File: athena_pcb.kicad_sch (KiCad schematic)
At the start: 29 parts, among them J1 Conn_02x03_Odd_Even, SW1 SW_Push, U1 NRF5340-QKAA-R7, U2 BME280, Y1 32MHz, Y2 32.768kHz

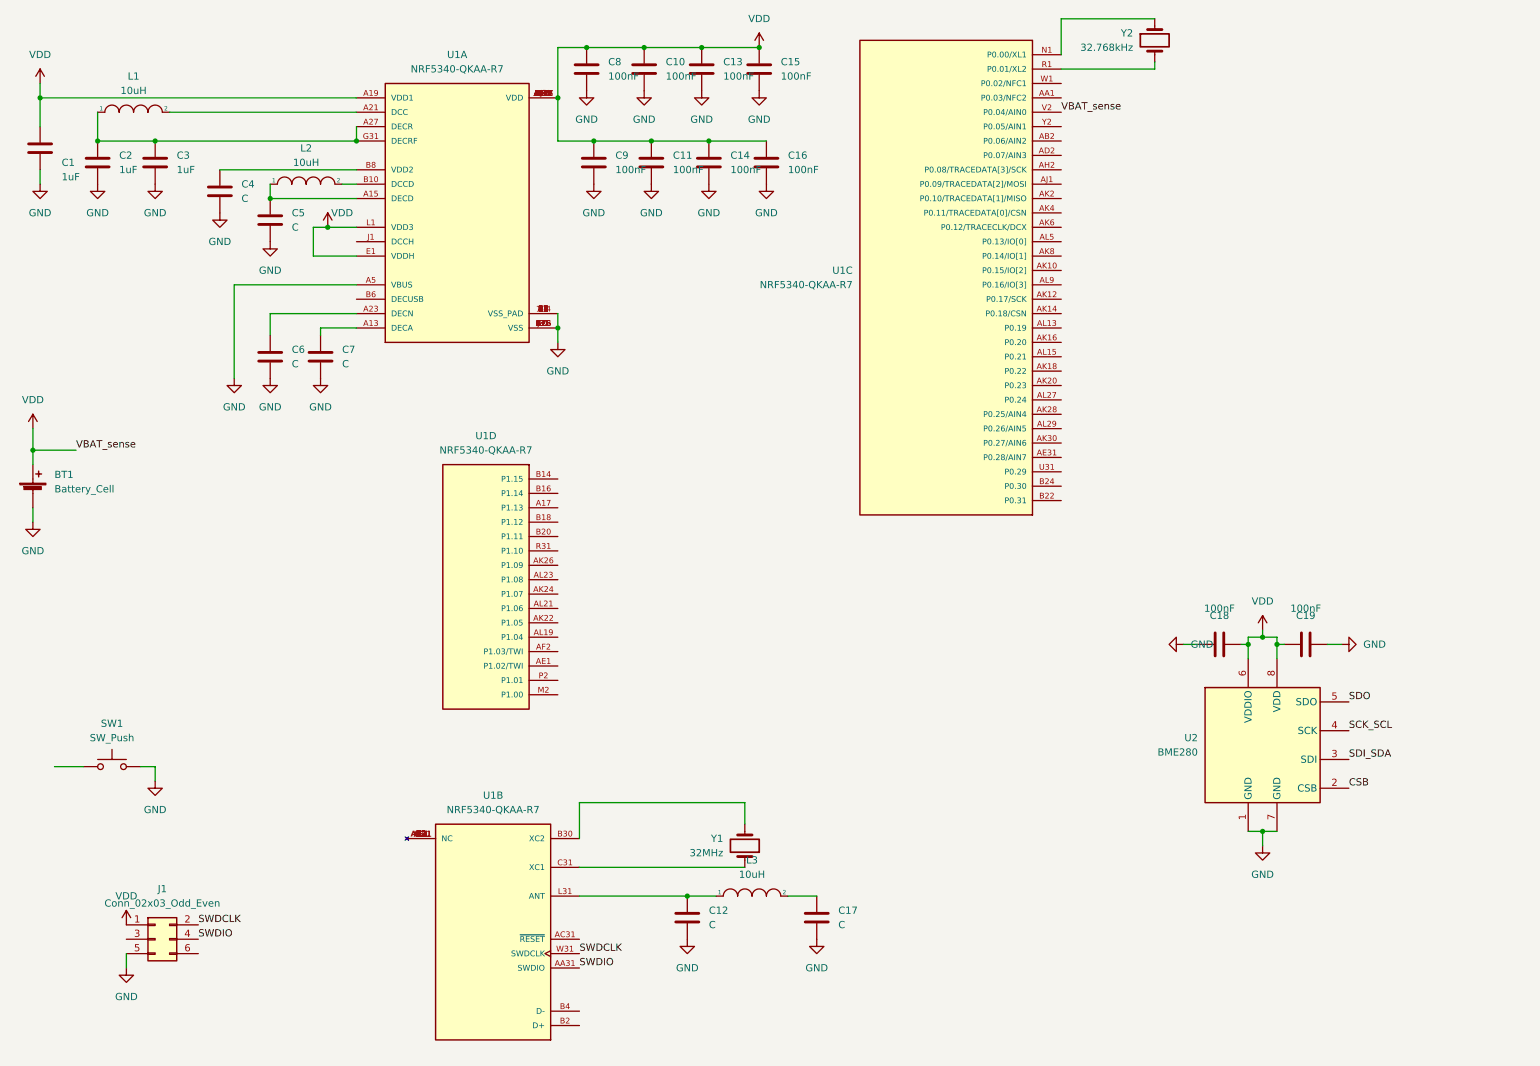
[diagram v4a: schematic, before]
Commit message: Added user button and indicator LED
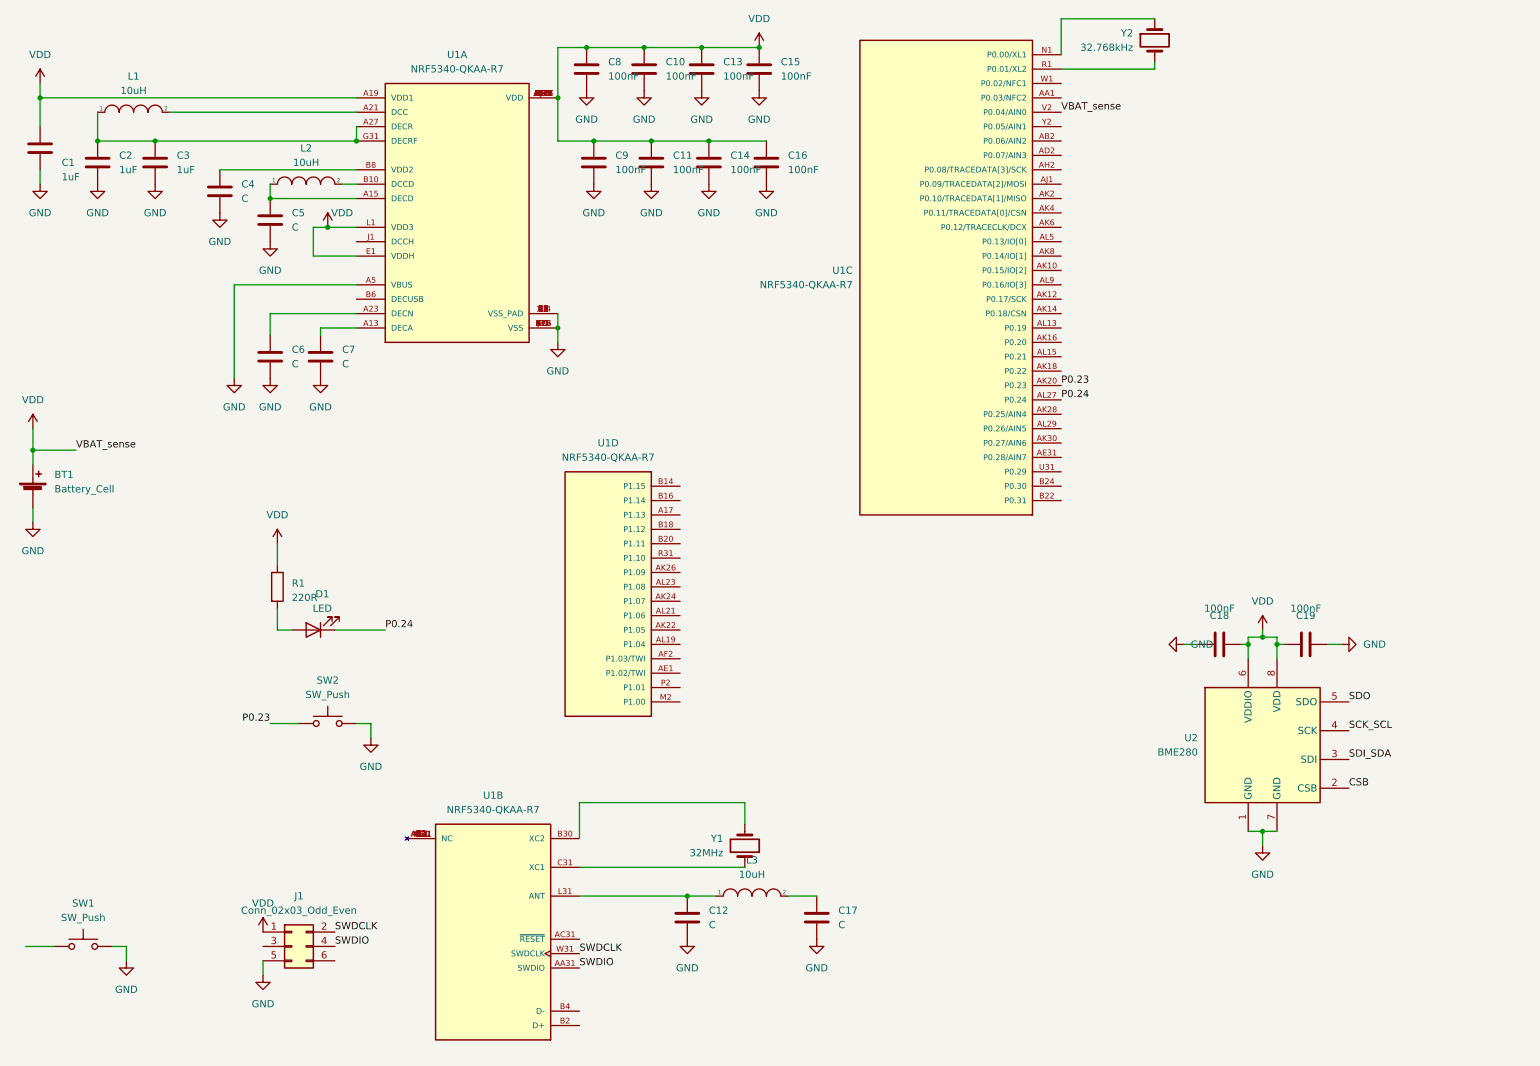
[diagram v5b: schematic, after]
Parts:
- added D1: LED, symbol Device:LED
- added R1: 220R, symbol Device:R
- added SW2: SW_Push, symbol Switch:SW_Push
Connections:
- net GND: now also SW2.2
- net VDD: now also R1.1
- net P0.23: now reaches U1.AK20 (P0.23)
- net P0.23: now also SW2.1
- net P0.24: now reaches U1.AL27 (P0.24)
- net P0.24: now also D1.1 (K)
- new net: D1.2 (A), R1.2
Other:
- moved on the sheet: J1, SW1, U1D

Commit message: Added footprint to capacitors
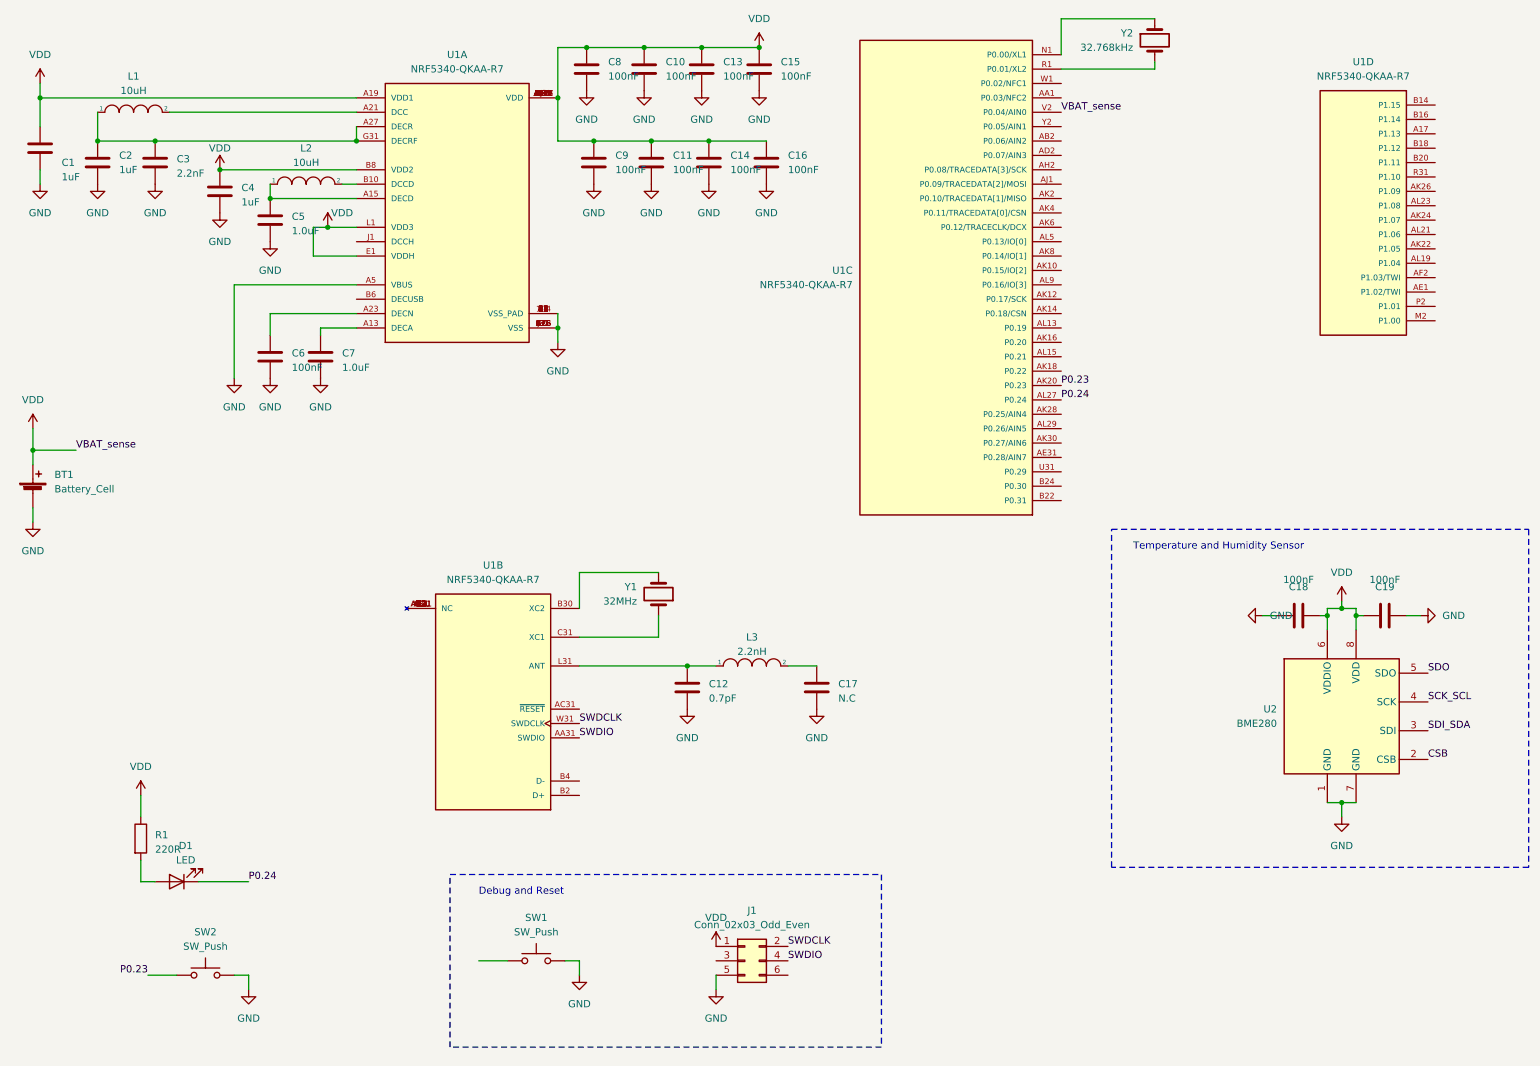
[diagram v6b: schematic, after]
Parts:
- C1, C2, C9: footprint (none) -> Capacitor_SMD:C_0402_1005Metric
- C10, C11, C13, C14, C15, C16, C18, C19, C8: footprint (none) -> Capacitor_SMD:C_0201_0603Metric
- C12: value C -> 0.7pF; footprint (none) -> Capacitor_SMD:C_0201_0603Metric
- C17: value C -> N.C; footprint (none) -> Capacitor_SMD:C_0201_0603Metric
- C3: value 1uF -> 2.2nF; footprint (none) -> Capacitor_SMD:C_0201_0603Metric
- C4: value C -> 1uF; footprint (none) -> Capacitor_SMD:C_0402_1005Metric
- C5, C7: value C -> 1.0uF; footprint (none) -> Capacitor_SMD:C_0402_1005Metric
- C6: value C -> 100nF; footprint (none) -> Capacitor_SMD:C_0201_0603Metric
- L3: value 10uH -> 2.2nH; footprint (none) -> Inductor_SMD:L_0201_0603Metric
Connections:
- net VDD: now also C4.1, U1.B8 (VDD2)
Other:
- note added: "Debug and Reset"
- note added: "Temperature and Humidity Sensor"
- moved on the sheet: C12, C17, C18, C19, D1, J1, L3, R1, SW1, SW2, U1B, U1D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

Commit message: Added footprint and symbol for the NRF53
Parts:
- BT1: footprint (none) -> Battery:BatteryHolder_Keystone_1060_1x2032
- D1: footprint (none) -> LED_SMD:LED_0402_1005Metric
- J1: footprint (none) -> Connector_PinHeader_1.27mm:PinHeader_2x03_P1.27mm_Vertical
- L1, L2: footprint (none) -> Inductor_SMD:L_0201_0603Metric
- R1: footprint (none) -> Resistor_SMD:R_0201_0603Metric
- SW1: footprint (none) -> Button_Switch_SMD:SW_Push_SPST_NO_Alps_SKRK
- SW2: footprint (none) -> Button_Switch_SMD:SW_Push_1P1T_NO_CK_KMR2
- Y1: footprint (none) -> Crystal:Crystal_SMD_2016-4Pin_2.0x1.6mm
- Y2: footprint (none) -> Crystal:Crystal_SMD_2012-2Pin_2.0x1.2mm
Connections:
- no-connect marks 0 -> 5
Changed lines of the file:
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@@
   (junction (at 116.84 19.05) (diameter 0) (color 0 0 0 0)
   )
+  (junction (at 111.76 71.12) (diameter 0) (color 0 0 0 0)
+  )
   (junction (at 52.07 40.64) (diameter 0) (color 0 0 0 0)
   )
@@
   (junction (at 19.05 90.17) (diameter 0) (color 0 0 0 0)
   )
+  (no_connect (at 76.2 63.5))
+  (no_connect (at 139.7 180.34))
+  (no_connect (at 76.2 53.34))
+  (no_connect (at 115.57 148.59))
+  (no_connect (at 115.57 151.13))
   (wire (pts (xy 200.66 22.86) (xy 217.17 22.86))
     (stroke (width 0) (type default))
@@
     (stroke (width 0) (type default))
   )
+  (wire (pts (xy 111.76 71.12) (xy 119.38 71.12))
+    (stroke (width 0) (type default))
+  )
   (wire (pts (xy 115.57 111.76) (xy 129.54 111.76))
     (stroke (width 0) (type default))
@@
     (stroke (width 0) (type default))
   )
+  (wire (pts (xy 57.15 110.49) (xy 57.15 114.3))
+    (stroke (width 0) (type default))
+  )
   (wire (pts (xy 128.27 35.56) (xy 138.43 35.56))
     (stroke (width 0) (type default))
@@
   )
   (wire (pts (xy 247.65 118.11) (xy 250.19 118.11))
+    (stroke (width 0) (type default))
+  )
+  (wire (pts (xy 48.26 105.41) (xy 48.26 109.22))
     (stroke (width 0) (type default))
   )
@@
     )
   )
+  (symbol (lib_id "power:PWR_FLAG") (at 119.38 71.12 270) (unit 1)
+    (in_bom yes) (on_board yes) (dnp no) (fields_autoplaced)
+    (property "Reference" "#FLG02" (at 121.285 71.12 0)
+      (effects (font (size 1.27 1.27)) hide)
+    )
+    (property "Value" "PWR_FLAG" (at 123.19 71.755 90)
+      (effects (font (size 1.27 1.27)) (justify left))
+    )
+    (property "Footprint" "" (at 119.38 71.12 0)
+      (effects (font (size 1.27 1.27)) hide)
+    )
+    (property "Datasheet" "~" (at 119.38 71.12 0)
+      (effects (font (size 1.27 1.27)) hide)
+    )
+    (pin "1")
+    (instances
+      (project "athena_pcb"
+        (path "/fadb6411-1081-41a3-ba72-837bcce93ee0"
+          (reference "#FLG02") (unit 1)
+        )
+      )
+    )
+  )
   (symbol (lib_id "power:GND") (at 148.59 43.18 0) (unit 1)
     (in_bom yes) (on_board yes) (dnp no) (fields_autoplaced)
@@
       (effects (font (size 1.27 1.27)))
     )
-    (property "Footprint" "" (at 67.31 43.18 0)
+    (property "Footprint" "Inductor_SMD:L_0201_0603Metric" (at 67.31 43.18 0)
       (effects (font (size 1.27 1.27)) hide)
     )
@@
       (effects (font (size 1.27 1.27)) (justify left))
     )
-    (property "Footprint" "" (at 19.05 96.266 90)
+    (property "Footprint" "Battery:BatteryHolder_Keystone_1060_1x2032" (at 19.05 96.266 90)
       (effects (font (size 1.27 1.27)) hide)
     )
@@
         (path "/fadb6411-1081-41a3-ba72-837bcce93ee0"
           (reference "BT1") (unit 1)
+        )
+      )
+    )
+  )
+  (symbol (lib_id "power:PWR_FLAG") (at 48.26 105.41 0) (unit 1)
+    (in_bom yes) (on_board yes) (dnp no) (fields_autoplaced)
+    (property "Reference" "#FLG03" (at 48.26 103.505 0)
+      (effects (font (size 1.27 1.27)) hide)
+    )
+    (property "Value" "PWR_FLAG" (at 48.26 101.6 0)
+      (effects (font (size 1.27 1.27)))
+    )
+    (property "Footprint" "" (at 48.26 105.41 0)
+      (effects (font (size 1.27 1.27)) hide)
+    )
+    (property "Datasheet" "~" (at 48.26 105.41 0)
+      (effects (font (size 1.27 1.27)) hide)
+    )
+    (pin "1")
+    (instances
+      (project "athena_pcb"
+        (path "/fadb6411-1081-41a3-ba72-837bcce93ee0"
+          (reference "#FLG03") (unit 1)
         )
       )
@@
       (effects (font (size 1.27 1.27)))
     )
-    (property "Footprint" "" (at 49.53 177.8 0)
+    (property "Footprint" "Button_Switch_SMD:SW_Push_1P1T_NO_CK_KMR2" (at 49.53 177.8 0)
       (effects (font (size 1.27 1.27)) hide)
     )
@@
     )
   )
+  (symbol (lib_id "power:VDD") (at 57.15 110.49 0) (unit 1)
+    (in_bom yes) (on_board yes) (dnp no) (fields_autoplaced)
+    (property "Reference" "#PWR036" (at 57.15 114.3 0)
+      (effects (font (size 1.27 1.27)) hide)
+    )
+    (property "Value" "VDD" (at 57.15 105.41 0)
+      (effects (font (size 1.27 1.27)))
+    )
+    (property "Footprint" "" (at 57.15 110.49 0)
+      (effects (font (size 1.27 1.27)) hide)
+    )
+    (property "Datasheet" "" (at 57.15 110.49 0)
+      (effects (font (size 1.27 1.27)) hide)
+    )
+    (pin "1")
+    (instances
+      (project "athena_pcb"
+        (path "/fadb6411-1081-41a3-ba72-837bcce93ee0"
+          (reference "#PWR036") (unit 1)
+        )
+      )
+    )
+  )
   (symbol (lib_id "power:VDD") (at 19.05 86.36 0) (unit 1)
     (in_bom yes) (on_board yes) (dnp no) (fields_autoplaced)
@@
       (effects (font (size 1.27 1.27)))
     )
-    (property "Footprint" "" (at 44.45 166.37 0)
+    (property "Footprint" "LED_SMD:LED_0402_1005Metric" (at 44.45 166.37 0)
       (effects (font (size 1.27 1.27)) hide)
     )
@@
       (effects (font (size 1.27 1.27)))
     )
-    (property "Footprint" "" (at 144.78 180.34 0)
+    (property "Footprint" "Connector_PinHeader_1.27mm:PinHeader_2x03_P1.27mm_Vertical" (at 144.78 180.34 0)
       (effects (font (size 1.27 1.27)) hide)
     )
@@
     )
   )
+  (symbol (lib_id "power:GND") (at 48.26 109.22 0) (unit 1)
+    (in_bom yes) (on_board yes) (dnp no) (fields_autoplaced)
+    (property "Reference" "#PWR035" (at 48.26 115.57 0)
+      (effects (font (size 1.27 1.27)) hide)
+    )
+    (property "Value" "GND" (at 48.26 114.3 0)
+      (effects (font (size 1.27 1.27)))
+    )
+    (property "Footprint" "" (at 48.26 109.22 0)
+      (effects (font (size 1.27 1.27)) hide)
+    )
+    (property "Datasheet" "" (at 48.26 109.22 0)
+      (effects (font (size 1.27 1.27)) hide)
+    )
+    (pin "1")
+    (instances
+      (project "athena_pcb"
+        (path "/fadb6411-1081-41a3-ba72-837bcce93ee0"
+          (reference "#PWR035") (unit 1)
+        )
+      )
+    )
+  )
   (symbol (lib_id "Switch:SW_Push") (at 107.95 180.34 0) (unit 1)
     (in_bom yes) (on_board yes) (dnp no) (fields_autoplaced)
@@
       (effects (font (size 1.27 1.27)))
     )
-    (property "Footprint" "" (at 107.95 175.26 0)
+    (property "Footprint" "Button_Switch_SMD:SW_Push_SPST_NO_Alps_SKRK" (at 107.95 175.26 0)
       (effects (font (size 1.27 1.27)) hide)
     )
@@
       (effects (font (size 1.27 1.27)) (justify left))
     )
-    (property "Footprint" "" (at 217.17 17.78 0)
+    (property "Footprint" "Crystal:Crystal_SMD_2012-2Pin_2.0x1.2mm" (at 217.17 17.78 0)
       (effects (font (size 1.27 1.27)) hide)
     )
@@
       (effects (font (size 1.27 1.27)))
     )
-    (property "Footprint" "" (at 36.83 30.48 0)
+    (property "Footprint" "Inductor_SMD:L_0201_0603Metric" (at 36.83 30.48 0)
       (effects (font (size 1.27 1.27)) hide)
     )
@@
       (effects (font (size 1.27 1.27)) (justify left))
     )
-    (property "Footprint" "" (at 36.322 158.75 90)
+    (property "Footprint" "Resistor_SMD:R_0201_0603Metric" (at 36.322 158.75 90)
       (effects (font (size 1.27 1.27)) hide)
     )
@@
       (effects (font (size 1.27 1.27)) (justify right))
     )
-    (property "Footprint" "" (at 129.54 115.57 0)
+    (property "Footprint" "Crystal:Crystal_SMD_2016-4Pin_2.0x1.6mm" (at 129.54 115.57 0)
       (effects (font (size 1.27 1.27)) hide)
     )
@@
         )
       )
+    )
+  )
+  (symbol (lib_id "power:PWR_FLAG") (at 57.15 114.3 180) (unit 1)
+    (in_bom yes) (on_board yes) (dnp no) (fields_autoplaced)
+    (property "Reference" "#FLG04" (at 57.15 116.205 0)
+      (effects (font (size 1.27 1.27)) hide)
+    )
+    (property "Value" "PWR_FLAG" (at 57.15 119.38 0)
+      (effects (font (size 1.27 1.27)))
+    )
+    (property "Footprint" "" (at 57.15 114.3 0)
+      (effects (font (size 1.27 1.27)) hide)
+    )
+    (property "Datasheet" "~" (at 57.15 114.3 0)
+      (effects (font (size 1.27 1.27)) hide)
+    )
+    (pin "1")
+    (instances
+      (project "athena_pcb"
+        (path "/fadb6411-1081-41a3-ba72-837bcce93ee0"
+          (reference "#FLG04") (unit 1)
+        )
+      )
